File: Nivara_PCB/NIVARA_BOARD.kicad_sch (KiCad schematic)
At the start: 3 parts, among them U18 ESP32-S3-WROOM-1

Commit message: New changes to the Nivara PCB schematic files.
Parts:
- added C16: 1uF, PCM_Capacitor_SMD_AKL:C_0603_1608Metric, symbol PCM_Capacitor_US_AKL:C_0603
- added C17: 22uF, PCM_Capacitor_SMD_AKL:C_0603_1608Metric, symbol PCM_Capacitor_US_AKL:C_0603
- added C18: 100nF, PCM_Capacitor_SMD_AKL:C_0603_1608Metric, symbol PCM_Capacitor_US_AKL:C_0603
- added R49: 10k, PCM_Resistor_SMD_AKL:R_0603_1608Metric, symbol PCM_Resistor_US_AKL:R_0603
- added SW1, SW2: Push_Button, Button_Switch_THT:SW_PUSH_6mm, symbol PCM_SL_Devices:Push_Button
- R1: value R_0603 -> 10k
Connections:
- net +3.3V: now also C16.1, C17.1, C18.1, R49.1
- net ANALOG_IN/ESP_4-20_IN: now also U18.4 (GPIO4/TOUCH4/ADC1_CH3)
- net ANALOG_IN/ESP_A0_10_IN_1: now also U18.6 (GPIO6/TOUCH6/ADC1_CH5)
- net ANALOG_IN/ESP_A0_32_IN_1: now also U18.5 (GPIO5/TOUCH5/ADC1_CH4)
- net D_IN/ESP_D_IN_1: now also U18.28 (SPIIO6/GPIO35/FSPID/SUBSPID)
- net D_IN/ESP_D_IN_2: now also U18.29 (SPIIO7/GPIO36/FSPICLK/SUBSPICLK)
- net D_IN/ESP_RUN_IN: now also U18.30 (SPIDQS/GPIO37/FSPIQ/SUBSPIQ)
- net GND1: now also C16.2, C17.2, C18.2, SW1.2, SW2.1
- net NPN_IN/ESP_NPN_IN_1: now also U18.32 (MTCK/GPIO39/CLK_OUT3/SUBSPICS1)
- net NPN_IN/ESP_NPN_IN_2: now also U18.33 (MTDO/GPIO40/CLK_OUT2)
- net NPN_OUT/ESP_NPN_OUT_1: now also U18.34 (MTDI/GPIO41/CLK_OUT1)
- net NPN_OUT/ESP_NPN_OUT_2: now also U18.35 (MTMS/GPIO42)
- net PNP_IN/ESP_PNP_IN_1: now also U18.8 (GPIO15/U0RTS/ADC2_CH4/XTAL_32K_P)
- net PNP_IN/ESP_PNP_IN_2: now also U18.9 (GPIO16/U0CTS/ADC2_CH5/XTAL_32K_N)
- net PNP_OUT/ESP_PNP_OUT_1: now also U18.23 (GPIO21)
- net PNP_OUT/ESP_PNP_OUT_2: now also U18.24 (GPIO47/SPICLK_P/SUBSPICLK_P_DIFF)
- net RELAY1&2/ESP_RLY2: now also U18.39 (GPIO1/TOUCH1/ADC1_CH0)
- net RELAY1&2/ESP_RY1: now also U18.38 (GPIO2/TOUCH2/ADC1_CH1)
- net ANALOG_OUT/SDA_C: now reaches U18.22 (GPIO14/TOUCH14/ADC2_CH3/FSPIWP/FSPIDQS/SUBSPIWP)
- net AUX_1: now reaches U18.25 (GPIO48/SPICLK_N/SUBSPICLK_N_DIFF)
- net AUX_2: now reaches U18.26 (GPIO45)
- net at U18.27 (GPIO0/BOOT): now also R49.2, SW1.1
- net at R1.2, U18.3 (EN): now also SW2.2
- net Vbus: now reaches U18.7 (GPIO7/TOUCH7/ADC1_CH6)
- net ESP_SEL_VOUT: no longer names the net of U18.17 (GPIO9/TOUCH9/ADC1_CH8/FSPIHD/SUBSPIHD)
- net SCLK_C renamed ANALOG_OUT/SDA_V
- net SCLK_V renamed ANALOG_OUT/ESP_SEL_VOUT
- net SDA_C renamed ANALOG_OUT/SCLK_C
- net SDA_V renamed ANALOG_OUT/SCLK_V
- net UART_IN renamed DRIVER_RS485/UART_IN
- net UART_OUT renamed DRIVER_RS485/UART_OUT
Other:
- moved on the sheet: C1

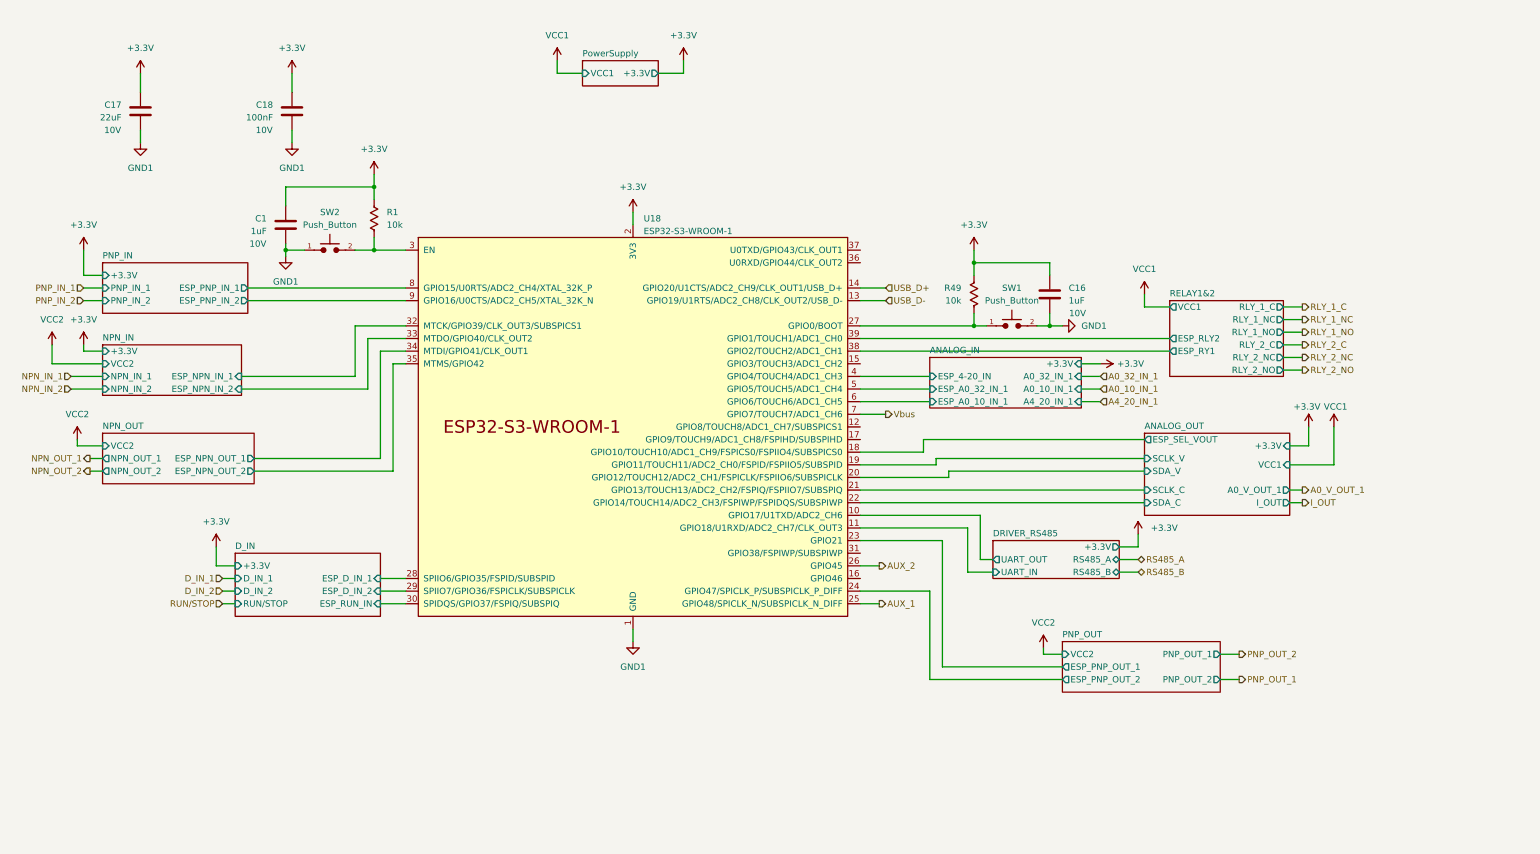
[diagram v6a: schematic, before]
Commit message: Cambios en el PCB de Nivara. Ruteo de emtradas y salidas NPN y PNP.
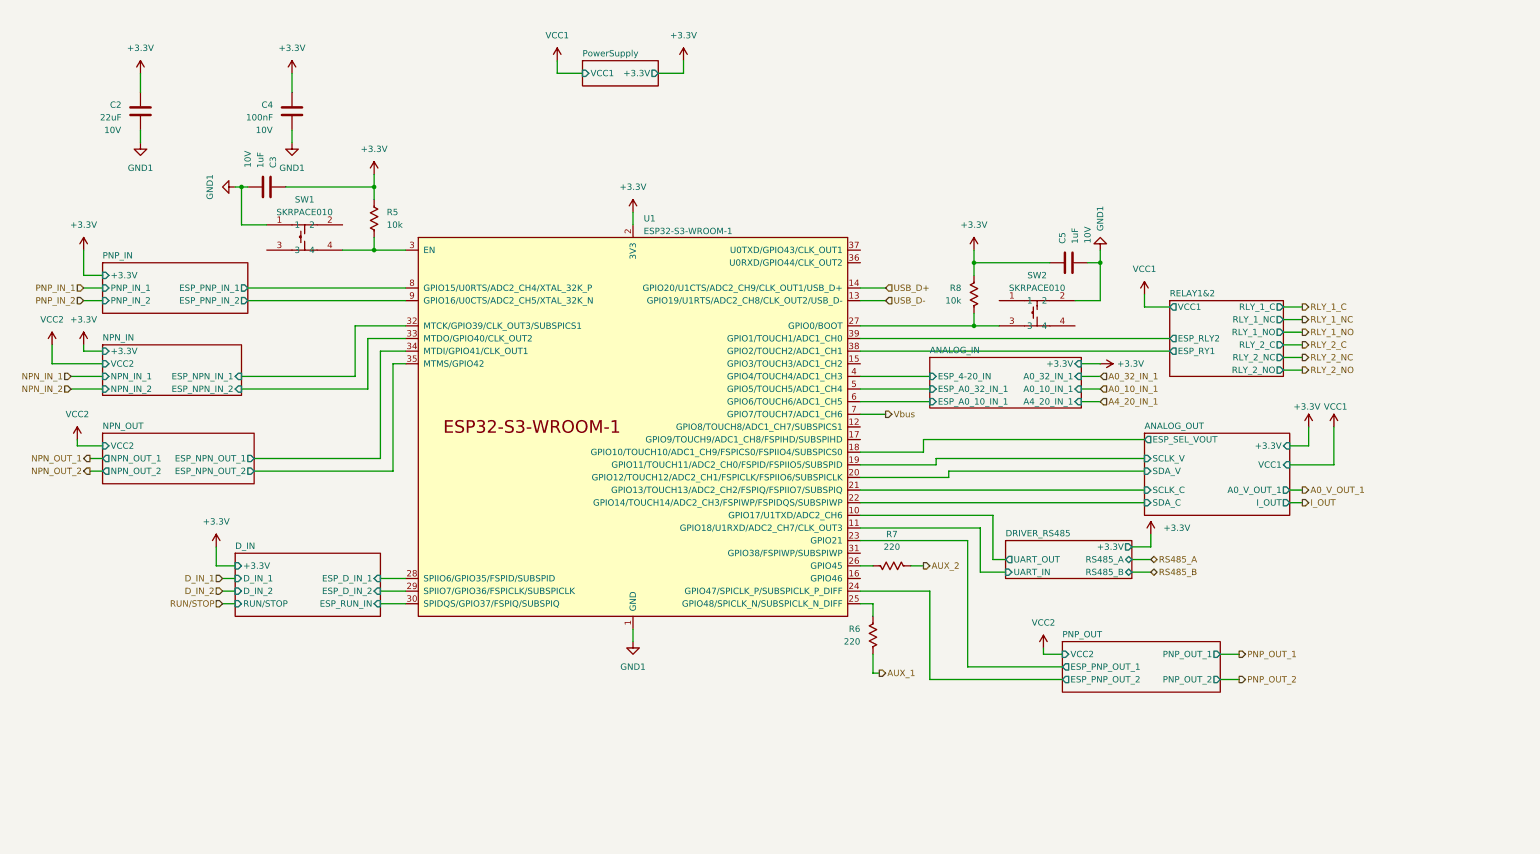
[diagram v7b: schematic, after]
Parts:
- removed SW1, SW2: Push_Button, Button_Switch_THT:SW_PUSH_6mm, symbol PCM_SL_Devices:Push_Button
- added R6, R7: 220, PCM_Resistor_SMD_AKL:R_0603_1608Metric, symbol PCM_Resistor_US_AKL:R_0603
- added SW1, SW2: SKRPACE010, EasyEDA:KEY-SMD_4P-L4.2-W3.2-P2.20-LS4.6, symbol EasyEDA:SKRPACE010
- renumbered C17 to C2, C1 to C3, C18 to C4, C16 to C5, R1 to R5, R49 to R8, U18 to U1
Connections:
- net AUX_1: now also R6.2; no longer U1.25 (GPIO48/SPICLK_N/SUBSPICLK_N_DIFF)
- net AUX_2: now also R7.2; no longer U1.26 (GPIO45)
- net GND1: now also SW1.1, SW2.2
- net at R8.2, U1.27 (GPIO0/BOOT): now also SW2.3
- net at R5.2, U1.3 (EN): now also SW1.4
- new net: R6.1, U1.25 (GPIO48/SPICLK_N/SUBSPICLK_N_DIFF)
- new net: R7.1, U1.26 (GPIO45)
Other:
- moved on the sheet: C3, C5

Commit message: Cambios realizados en el PCB y el esquema de Nivara_PCB.
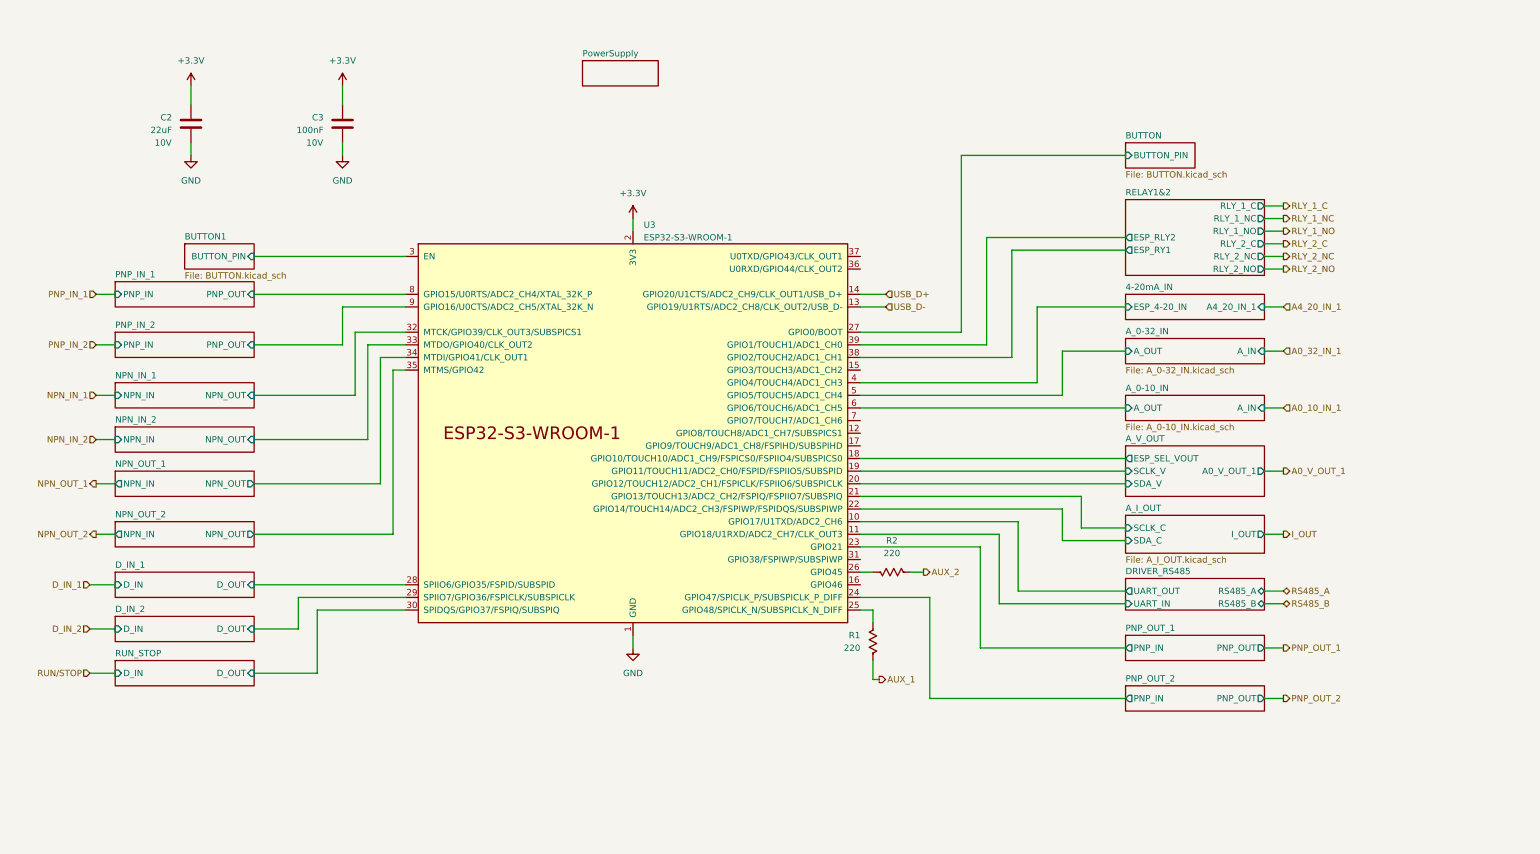
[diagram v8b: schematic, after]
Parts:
- removed C3, C5: 1uF, PCM_Capacitor_SMD_AKL:C_0603_1608Metric, symbol PCM_Capacitor_US_AKL:C_0603
- removed R5, R8: 10k, PCM_Resistor_SMD_AKL:R_0603_1608Metric, symbol PCM_Resistor_US_AKL:R_0603
- removed SW1, SW2: SKRPACE010, EasyEDA:KEY-SMD_4P-L4.2-W3.2-P2.20-LS4.6, symbol EasyEDA:SKRPACE010
- renumbered C4 to C3, R6 to R1, R7 to R2, U1 to U3
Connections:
- net BUTTON/BUTTON_PIN: now reaches U3.27 (GPIO0/BOOT)
- net BUTTON1/BUTTON_PIN: now reaches U3.3 (EN)
- net 4-20mA_IN/ESP_A0_10_IN_1 renamed A_0-10_IN/A_OUT
- net 4-20mA_IN/ESP_A0_32_IN_1 renamed A_0-32_IN/A_OUT
- net A_V_OUT/SCLK_C renamed A_I_OUT/SCLK_C
- net A_V_OUT/SDA_C renamed A_I_OUT/SDA_C
- net D_IN_1/ESP_D_IN_1 renamed D_IN_1/D_OUT
- net D_IN_1/ESP_D_IN_2 renamed D_IN_2/D_OUT
- net D_IN_1/ESP_RUN_IN renamed RUN_STOP/D_OUT
- net GND1 renamed GND
- net NPN_IN_1/ESP_NPN_IN_1 renamed NPN_IN_1/NPN_OUT
- net NPN_IN_1/ESP_NPN_IN_2 renamed NPN_IN_2/NPN_OUT
- net NPN_OUT_1/ESP_NPN_OUT_1 renamed NPN_OUT_1/NPN_OUT
- net NPN_OUT_1/ESP_NPN_OUT_2 renamed NPN_OUT_2/NPN_OUT
- net PNP_IN_1/ESP_PNP_IN_1 renamed PNP_IN_1/PNP_OUT
- net PNP_IN_1/ESP_PNP_IN_2 renamed PNP_IN_2/PNP_OUT
- net PNP_OUT_1/ESP_PNP_OUT_1 renamed PNP_OUT_1/PNP_IN
- net PNP_OUT_1/ESP_PNP_OUT_2 renamed PNP_OUT_2/PNP_IN
- net Vbus: no longer names the net of U3.7 (GPIO7/TOUCH7/ADC1_CH6)
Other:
- sheet ANALOG_IN renamed 4-20mA_IN
- sheet ANALOG_OUT renamed A_V_OUT
- sheet D_IN renamed D_IN_1
- sheet NPN_IN renamed NPN_IN_1
- sheet NPN_OUT renamed NPN_OUT_1
- sheet PNP_IN renamed PNP_IN_1
- sheet PNP_OUT renamed PNP_OUT_1
- added sheet A_0-10_IN (A_0-10_IN.kicad_sch)
- added sheet A_0-32_IN (A_0-32_IN.kicad_sch)
- added sheet A_I_OUT (A_I_OUT.kicad_sch)
- added sheet BUTTON (BUTTON.kicad_sch)
- added sheet BUTTON1 (BUTTON.kicad_sch)
- added sheet D_IN_2 (D_IN.kicad_sch)
- added sheet NPN_IN_2 (NPN_IN.kicad_sch)
- added sheet NPN_OUT_2 (NPN_OUT.kicad_sch)
- added sheet PNP_IN_2 (PNP_IN.kicad_sch)
- added sheet PNP_OUT_2 (PNP_OUT.kicad_sch)
- added sheet RUN_STOP (D_IN.kicad_sch)
- sheet 4-20mA_IN ports: added none; removed +3.3V, A0_10_IN_1, A0_32_IN_1, ESP_A0_10_IN_1, ESP_A0_32_IN_1
- sheet A_V_OUT: file ANALOG_OUT.kicad_sch -> A_V_OUT.kicad_sch
- sheet A_V_OUT ports: added none; removed +3.3V, I_OUT, SCLK_C, SDA_C, VCC1
- sheet DRIVER_RS485 ports: added none; removed +3.3V
- sheet D_IN_1 ports: added D_IN, D_OUT; removed +3.3V, D_IN_1, D_IN_2, ESP_D_IN_1, ESP_D_IN_2, ESP_RUN_IN, RUN/STOP
- sheet NPN_IN_1 ports: added NPN_IN, NPN_OUT; removed +3.3V, ESP_NPN_IN_1, ESP_NPN_IN_2, NPN_IN_1, NPN_IN_2, VCC2
- sheet NPN_OUT_1 ports: added NPN_IN, NPN_OUT; removed ESP_NPN_OUT_1, ESP_NPN_OUT_2, NPN_OUT_1, NPN_OUT_2, VCC2
- sheet PNP_IN_1 ports: added PNP_IN, PNP_OUT; removed +3.3V, ESP_PNP_IN_1, ESP_PNP_IN_2, PNP_IN_1, PNP_IN_2
- sheet PNP_OUT_1 ports: added PNP_IN, PNP_OUT; removed ESP_PNP_OUT_1, ESP_PNP_OUT_2, PNP_OUT_1, PNP_OUT_2, VCC2
- sheet PowerSupply ports: added none; removed +3.3V, VCC1
- sheet RELAY1&2 ports: added none; removed VCC1
- moved on the sheet: C2, C3, R1, R2, U3
